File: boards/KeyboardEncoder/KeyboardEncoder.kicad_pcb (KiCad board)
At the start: 2 copper layers, 150 x 100 mm, 30 parts, among them J1 ISP, J2 Encoder, J3 MIDI Out, J4 SelectRX, J5 MIDI In, J7 BoardCon, J8 PistonEncoder, U1 ATmega48-20P, U2 6N137, U3 74LS14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

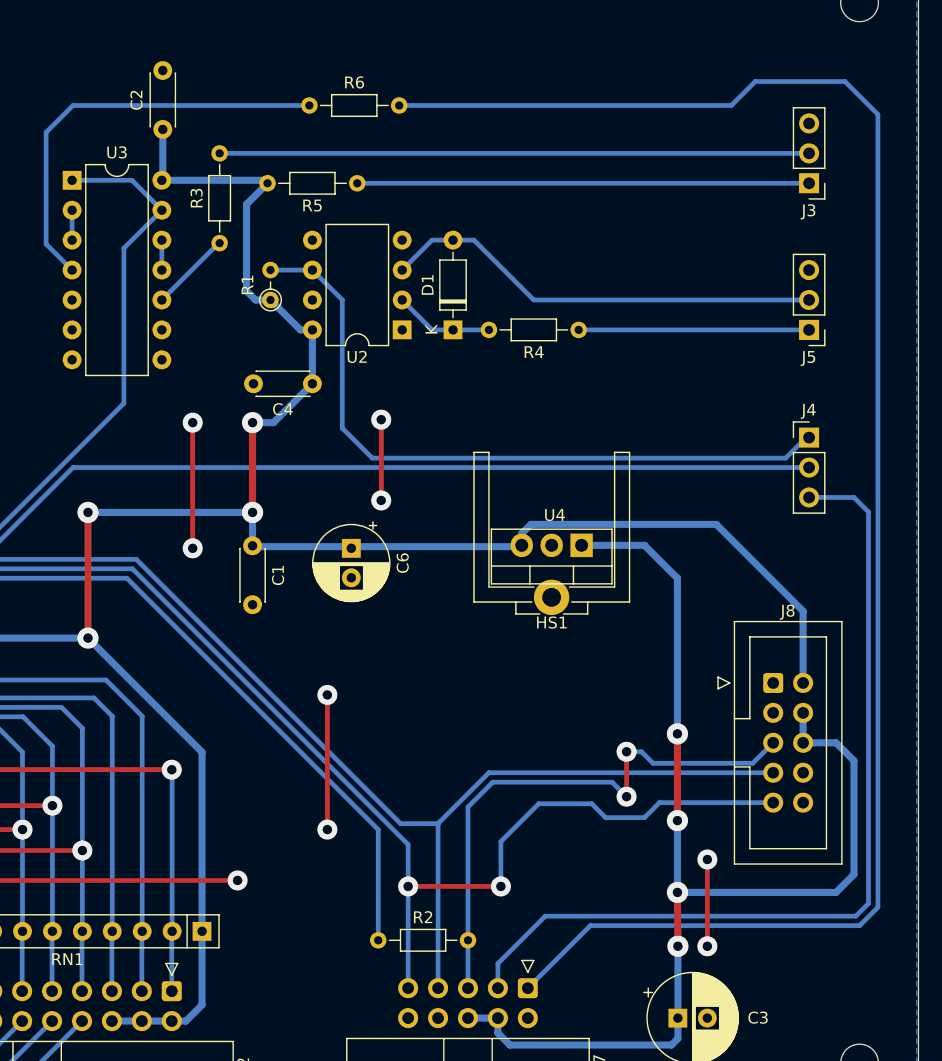
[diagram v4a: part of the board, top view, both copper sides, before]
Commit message: Finished IO-Board PCB, switched RX/TX of board connectors for better routing
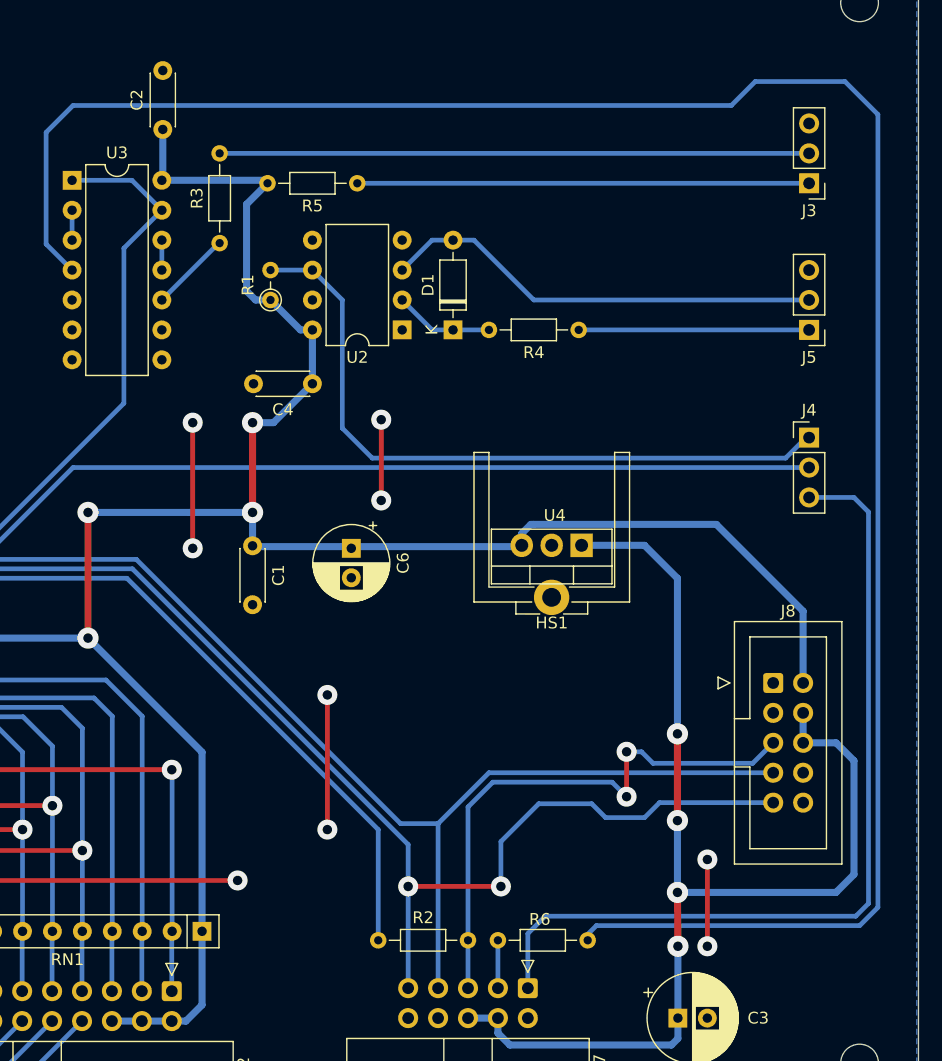
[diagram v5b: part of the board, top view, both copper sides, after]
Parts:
- moved R6 74.7 mm to (193.8, 129.8), turned to 180 degrees
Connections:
- J7 pad 1: TXT_OUT -> Ctrl In
- J7 pad 3: Ctrl In -> TXT_OUT
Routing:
- net Net-(R6-Pad1): track 35.9 -> 179.6 mm
- net TXT_OUT: track 142.5 -> 4.06 mm
- net Ctrl In: track 74.4 -> 73.4 mm
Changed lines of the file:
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@@
 	(footprint "Resistor_THT:R_Axial_DIN0204_L3.6mm_D1.6mm_P7.62mm_Horizontal"
 		(layer "F.Cu")
-		(at 170.18 58.928)
+		(at 193.802 129.794 180)
 		(descr "Resistor, Axial_DIN0204 series, Axial, Horizontal, pin pitch=7.62mm, 0.167W, length*diameter=3.6*1.6mm^2, http://cdn-reichelt.de/documents/datenblatt/B400/1_4W%23YAG.pdf")
 		(tags "Resistor Axial_DIN0204 series Axial Horizontal pin pitch 7.62mm 0.167W length 3.6mm diameter 1.6mm")
 		(property "Reference" "R6"
-			(at 3.81 -1.92 0)
+			(at 4.064 1.778 180)
 			(layer "F.SilkS")
 			(effects
@@
 		)
 		(property "Value" "220"
-			(at 3.81 1.92 0)
+			(at 3.81 -1.778 180)
 			(layer "F.Fab")
 			(effects
@@
 		)
 		(property "Footprint" "Resistor_THT:R_Axial_DIN0204_L3.6mm_D1.6mm_P7.62mm_Horizontal"
-			(at 0 0 0)
+			(at 0 0 180)
 			(unlocked yes)
 			(layer "F.Fab")
@@
 		)
 		(property "Datasheet" ""
-			(at 0 0 0)
+			(at 0 0 180)
 			(unlocked yes)
 			(layer "F.Fab")
@@
 		)
 		(property "Description" "Resistor"
-			(at 0 0 0)
+			(at 0 0 180)
 			(unlocked yes)
 			(layer "F.Fab")
@@
 		(attr through_hole)
 		(fp_line
-			(start 0.94 0)
-			(end 1.89 0)
+			(start 6.68 0)
+			(end 5.73 0)
 			(stroke
 				(width 0.12)
@@
 		)
 		(fp_line
-			(start 1.89 -0.92)
-			(end 1.89 0.92)
+			(start 5.73 0.92)
+			(end 5.73 -0.92)
 			(stroke
 				(width 0.12)
@@
 		)
 		(fp_line
-			(start 1.89 0.92)
-			(end 5.73 0.92)
+			(start 5.73 -0.92)
+			(end 1.89 -0.92)
 			(stroke
 				(width 0.12)
@@
 		)
 		(fp_line
-			(start 5.73 -0.92)
-			(end 1.89 -0.92)
+			(start 1.89 0.92)
+			(end 5.73 0.92)
 			(stroke
 				(width 0.12)
@@
 		)
 		(fp_line
-			(start 5.73 0.92)
-			(end 5.73 -0.92)
+			(start 1.89 -0.92)
+			(end 1.89 0.92)
 			(stroke
 				(width 0.12)
@@
 		)
 		(fp_line
-			(start 6.68 0)
-			(end 5.73 0)
+			(start 0.94 0)
+			(end 1.89 0)
 			(stroke
 				(width 0.12)
@@
 		)
 		(fp_line
-			(start -0.95 -1.05)
-			(end -0.95 1.05)
+			(start 8.57 1.05)
+			(end 8.57 -1.05)
 			(stroke
 				(width 0.05)
@@
 		)
 		(fp_line
-			(start -0.95 1.05)
-			(end 8.57 1.05)
+			(start 8.57 -1.05)
+			(end -0.95 -1.05)
 			(stroke
 				(width 0.05)
@@
 		)
 		(fp_line
-			(start 8.57 -1.05)
-			(end -0.95 -1.05)
+			(start -0.95 1.05)
+			(end 8.57 1.05)
 			(stroke
 				(width 0.05)
@@
 		)
 		(fp_line
-			(start 8.57 1.05)
-			(end 8.57 -1.05)
+			(start -0.95 -1.05)
+			(end -0.95 1.05)
 			(stroke
 				(width 0.05)
@@
 		)
 		(fp_line
-			(start 0 0)
-			(end 2.01 0)
+			(start 7.62 0)
+			(end 5.61 0)
 			(stroke
 				(width 0.1)
@@
 		)
 		(fp_line
-			(start 2.01 -0.8)
-			(end 2.01 0.8)
+			(start 5.61 0.8)
+			(end 5.61 -0.8)
 			(stroke
 				(width 0.1)
@@
 		)
 		(fp_line
-			(start 2.01 0.8)
-			(end 5.61 0.8)
+			(start 5.61 -0.8)
+			(end 2.01 -0.8)
 			(stroke
 				(width 0.1)
@@
 		)
 		(fp_line
-			(start 5.61 -0.8)
-			(end 2.01 -0.8)
+			(start 2.01 0.8)
+			(end 5.61 0.8)
 			(stroke
 				(width 0.1)
@@
 		)
 		(fp_line
-			(start 5.61 0.8)
-			(end 5.61 -0.8)
+			(start 2.01 -0.8)
+			(end 2.01 0.8)
 			(stroke
 				(width 0.1)
@@
 		)
 		(fp_line
-			(start 7.62 0)
-			(end 5.61 0)
+			(start 0 0)
+			(end 2.01 0)
 			(stroke
 				(width 0.1)
@@
 		)
 		(fp_text user "${REFERENCE}"
-			(at 3.81 0 0)
+			(at 3.81 0 180)
 			(layer "F.Fab")
 			(effects
@@
 		)
 		(pad "1" thru_hole circle
-			(at 0 0)
+			(at 0 0 180)
 			(size 1.4 1.4)
 			(drill 0.7)
@@
 		)
 		(pad "2" thru_hole oval
-			(at 7.62 0)
+			(at 7.62 0 180)
 			(size 1.4 1.4)
 			(drill 0.7)
@@
 			(remove_unused_layers no)
 			(roundrect_rratio 0.147059)
-			(net 41 "TXT_OUT")
+			(net 24 "Ctrl In")
 			(pinfunction "Pin_1")
 			(pintype "passive")
@@
 			(layers "*.Cu" "*.Mask")
 			(remove_unused_layers no)
-			(net 24 "Ctrl In")
+			(net 41 "TXT_OUT")
 			(pinfunction "Pin_3")
 			(pintype "passive")
@@
 	)
 	(segment
-		(start 190.199522 127.748)
-		(end 216.56063 127.748)
+		(start 188.722 133.858)
+		(end 188.722 129.225522)
 		(width 0.4)
 		(layer "B.Cu")
@@
 	)
 	(segment
-		(start 186.182 131.765522)
-		(end 190.199522 127.748)
+		(start 190.199522 127.748)
+		(end 216.56063 127.748)
 		(width 0.4)
 		(layer "B.Cu")
@@
 	)
 	(segment
-		(start 186.182 133.858)
-		(end 186.182 131.765522)
+		(start 217.64 126.66863)
+		(end 217.64 93.434)
 		(width 0.4)
 		(layer "B.Cu")
@@
 	)
 	(segment
-		(start 217.64 126.66863)
-		(end 217.64 93.434)
+		(start 188.722 129.225522)
+		(end 190.199522 127.748)
 		(width 0.4)
 		(layer "B.Cu")
@@
 	)
 	(segment
-		(start 215.646 56.896)
-		(end 208.026 56.896)
+		(start 186.182 129.794)
+		(end 186.182 133.858)
 		(width 0.4)
 		(layer "B.Cu")
@@
 	)
 	(segment
-		(start 177.8 58.928)
-		(end 205.994 58.928)
+		(start 162.48 70.612)
+		(end 162.56 70.612)
 		(width 0.4)
 		(layer "B.Cu")
-		(net 41)
+		(net 42)
 	)
 	(segment
-		(start 218.44 59.69)
-		(end 215.646 56.896)
+		(start 157.654 75.438)
+		(end 162.48 70.612)
 		(width 0.4)
 		(layer "B.Cu")
-		(net 41)
+		(net 42)
 	)
 	(segment
-		(start 188.722 133.858)
-		(end 194.032 128.548)
+		(start 157.654 70.358)
+		(end 157.654 72.898)
 		(width 0.4)
 		(layer "B.Cu")
-		(net 41)
+		(net 45)
 	)
 	(segment
-		(start 208.026 56.896)
-		(end 205.994 58.928)
+		(start 150.034 70.358)
+		(end 150.034 67.818)
 		(width 0.4)
 		(layer "B.Cu")
-		(net 41)
+		(net 46)
 	)
 	(segment
-		(start 216.892 128.548)
-		(end 218.44 127)
+		(start 147.828 61.214)
+		(end 147.828 70.692)
 		(width 0.4)
 		(layer "B.Cu")
-		(net 41)
+		(net 50)
+	)
+	(segment
+		(start 215.646 56.896)
+		(end 208.026 56.896)
+		(width 0.4)
+		(layer "B.Cu")
+		(net 50)
 	)
 	(segment
-		(start 194.032 128.548)
+		(start 194.54 128.548)
 		(end 216.892 128.548)
 		(width 0.4)
 		(layer "B.Cu")
-		(net 41)
+		(net 50)
+	)
+	(segment
+		(start 208.026 56.896)
+		(end 205.994 58.928)
+		(width 0.4)
+		(layer "B.Cu")
+		(net 50)
 	)
 	(segment
-		(start 218.44 127)
+		(start 218.44 127.000001)
 		(end 218.44 59.69)
 		(width 0.4)
 		(layer "B.Cu")
-		(net 41)
+		(net 50)
 	)
 	(segment
-		(start 162.48 70.612)
-		(end 162.56 70.612)
+		(start 193.802 129.794)
+		(end 193.802 129.286)
 		(width 0.4)
 		(layer "B.Cu")
-		(net 42)
+		(net 50)
 	)
 	(segment
-		(start 157.654 75.438)
-		(end 162.48 70.612)
+		(start 216.892 128.548)
+		(end 218.44 127.000001)
 		(width 0.4)
 		(layer "B.Cu")
-		(net 42)
+		(net 50)
 	)
 	(segment
-		(start 157.654 70.358)
-		(end 157.654 72.898)
+		(start 193.802 129.286)
+		(end 194.54 128.548)
 		(width 0.4)
 		(layer "B.Cu")
-		(net 45)
+		(net 50)
 	)
 	(segment
-		(start 150.034 70.358)
-		(end 150.034 67.818)
+		(start 218.44 59.69)
+		(end 215.646 56.896)
 		(width 0.4)
 		(layer "B.Cu")
-		(net 46)
+		(net 50)
 	)
 	(segment
@@
 	)
 	(segment
-		(start 170.18 58.928)
+		(start 205.994 58.928)
 		(end 150.114 58.928)
 		(width 0.4)
@@
 		(width 0.4)
 		(layer "B.Cu")
-		(net 50)
-	)
-	(segment
-		(start 147.828 61.214)
-		(end 147.828 70.692)
-		(width 0.4)
-		(layer "B.Cu")

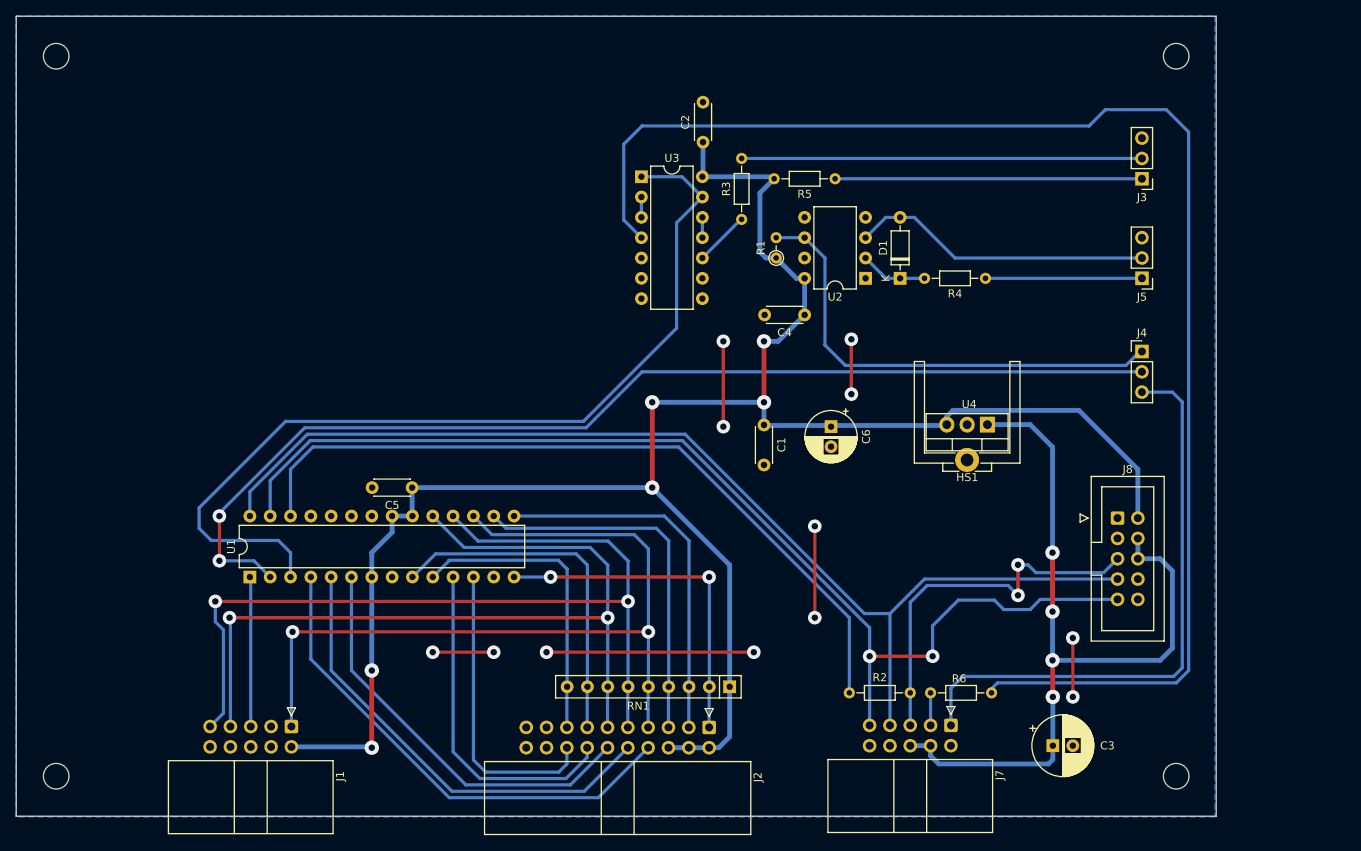
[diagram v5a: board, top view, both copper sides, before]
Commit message: Fixed interrupt line to use open collector, added pullups to I2C lines
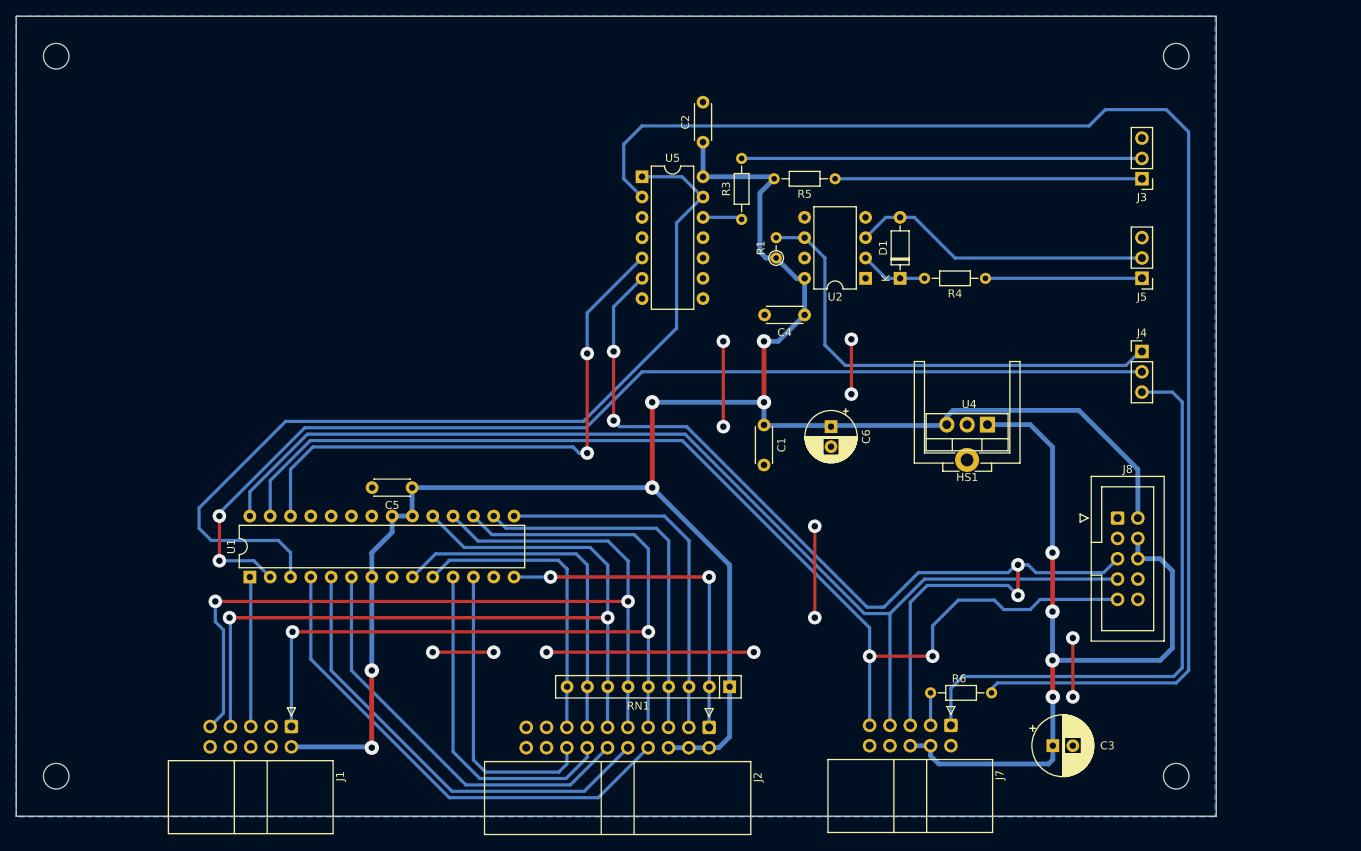
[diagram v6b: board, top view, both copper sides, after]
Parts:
- removed R2: 220, Resistor_THT:R_Axial_DIN0204_L3.6mm_D1.6mm_P7.62mm_Horizontal
- removed U3: 74LS14, Package_DIP:DIP-14_W7.62mm
- added U5: 74LS07, Package_DIP:DIP-14_W7.62mm, F.Cu at (150.1, 65.3)
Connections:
- net TXT_OUT renamed MIDI_OUT
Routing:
- net Net-(J7-Pin_5): track 47.6 -> 129.3 mm, vias 2 -> 4
- net Interrupt: track 95.1 -> 71.6 mm, vias 0 -> 2
- net Net-(R6-Pad1): track 179.6 -> 174.5 mm
- net Net-(U3-Pad2): track 2.54 -> 0.00 mm
- net Net-(U3-Pad11): track 2.54 -> 0.00 mm
- net Net-(R3-Pad1): track 6.90 -> 5.01 mm
